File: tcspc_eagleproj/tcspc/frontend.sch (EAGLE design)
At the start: 91 parts, among them Q2 ALD1101SAL, U1 DS90LV028AQ, U3 ADCMP582, U4 LT6003_SOT23-5, U5 LT6003_SOT23-5, U6 AD53X8, X1 SMA, X2 SMA

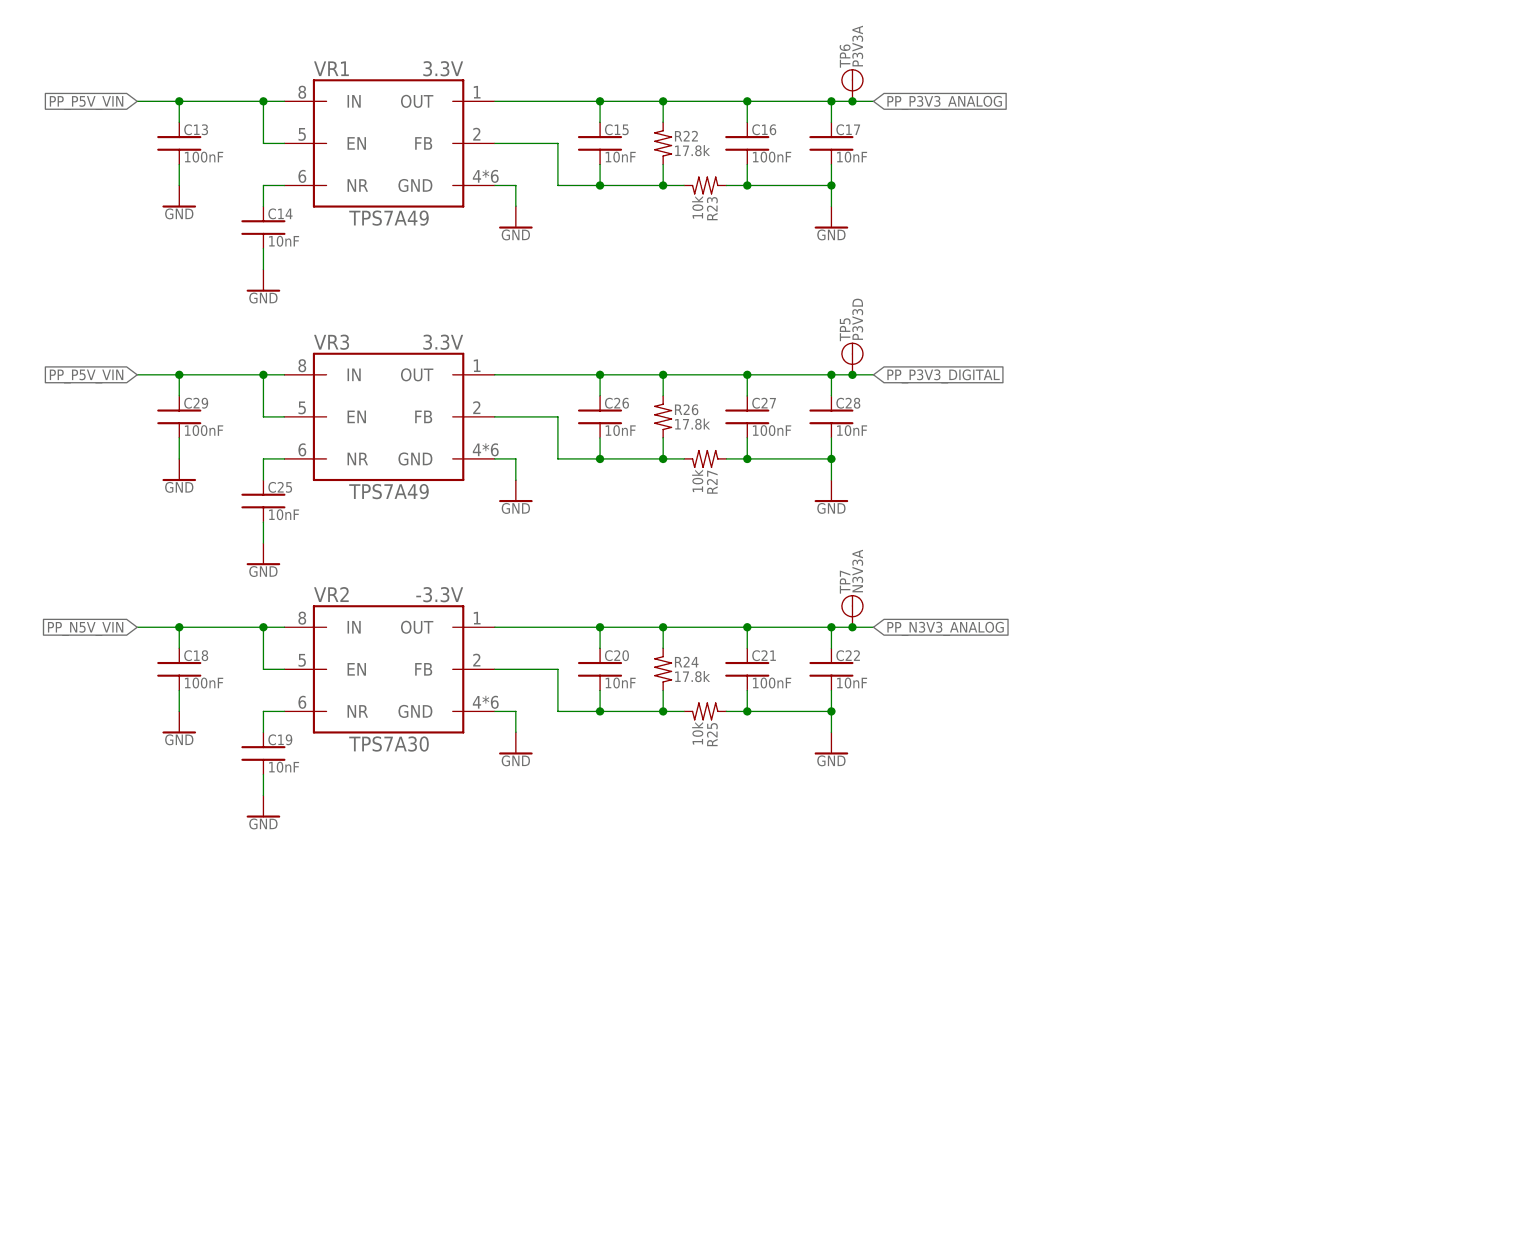
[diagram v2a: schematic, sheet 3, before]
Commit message: stuffed another datasheet into the folder, made some small tweaks to the schematic, created a new brd file and started organizing parts for routing. Fixed the small dot test pad and added a small drill in it for a scope probe
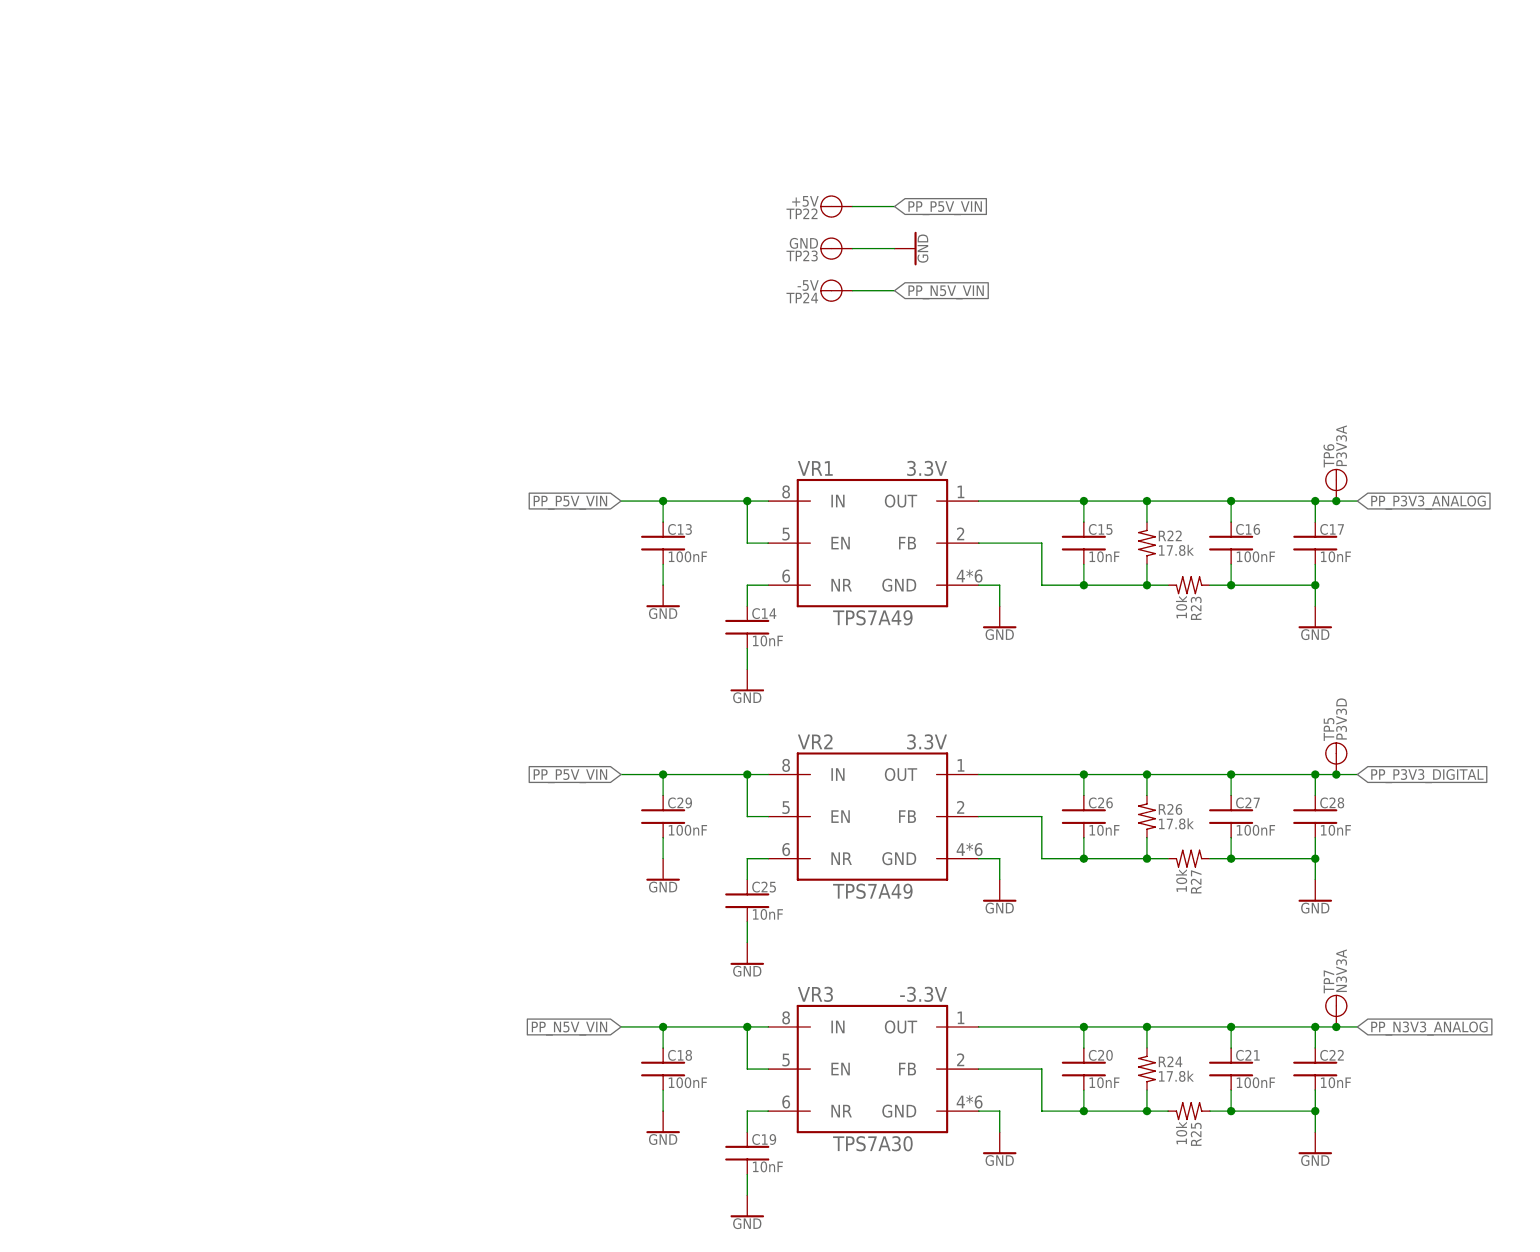
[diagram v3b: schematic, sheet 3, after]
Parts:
- added C4: 100nF, tcspc_lib:CAP_0402
- added TP22: +5V, tcspc_lib:TESTPOINT_A
- added TP23: GND, tcspc_lib:TESTPOINT_A
- added TP24: -5V, tcspc_lib:TESTPOINT_A
- R10, R11: value (none) -> 3.2k
- R12, R13: value (none) -> 1.8k
- R6: value 0 -> 1k
- TP1: value (none) -> DAC_SCLK
- TP18, TP19, TP20, TP21: device tcspc_lib:TESTPOINT_A -> tcspc_lib:TESTPOINT_PAD
- TP2: value (none) -> DAC_!SYNC!
- TP3: value (none) -> DAC_DIN
- TP4: value (none) -> DAC_!LDAC!
- TP8, TP9: value (none) -> GND
- VR2: value -3.3V -> 3.3V; device tcspc_lib:TPS7A30 -> tcspc_lib:TPS7A49
- VR3: value 3.3V -> -3.3V; device tcspc_lib:TPS7A49 -> tcspc_lib:TPS7A30
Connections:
- removed net N$15: U1.OUT-A, X2.1
- removed net N$20: TP9.TP
- new net N$14: U1.OUT-B, X2.1
- new net N$17: C55.1, R6.2, U5.IN+
- net !CHA_LVDS_OUT: now also U1.!IN-B; no longer U1.!IN-A
- net CHA_HYS_SET: now also R6.1; no longer C55.1, U5.IN+
- net CHA_LVDS_OUT: now also U1.IN-B; no longer U1.IN-A
- net CHA_THRESH_SET: now also R5.1; no longer R6.1
- net GND: now also C4.2, TP23.TP, TP8.TP, TP9.TP; no longer R5.2
- net N$16: now also VR2.NR; no longer VR3.NR
- net N$21: now also VR2.FB; no longer VR3.FB
- net N$25: now also VR3.NR; no longer VR2.NR
- net N$4: now also VR3.FB; no longer VR2.FB
- net N$9: now also R5.2; no longer R5.1, R6.2
- net PP_N3V3_ANALOG: now also C4.1, VR3.OUT; no longer VR2.OUT
- net PP_N5V_VIN: now also TP24.TP, VR3.EN, VR3.IN; no longer VR2.EN, VR2.IN
- net PP_P3V3_ANALOG: no longer C11.1
- net PP_P3V3_DIGITAL: now also C11.1, VR2.OUT; no longer VR3.OUT
- net PP_P5V_VIN: now also TP22.TP, VR2.EN, VR2.IN; no longer VR3.EN, VR3.IN
- net T/H_DAC_DIN: no longer TP8.TP
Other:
- moved on the sheet: C11, C12, C13, C14, C15, C16, C17, C18, C19, C20, C21, C22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

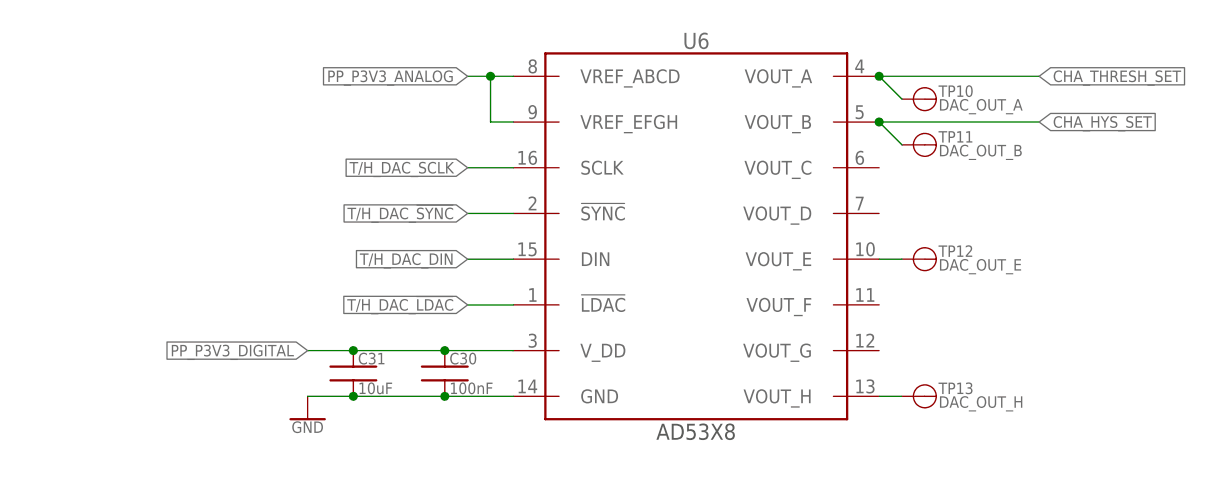
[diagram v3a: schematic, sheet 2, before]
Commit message: Added a termination resistor to the LVDS to TTL reciever, changed a few layers on the SMA coax connector, finished up the board layout, generated gerbers to send to 3PCB.
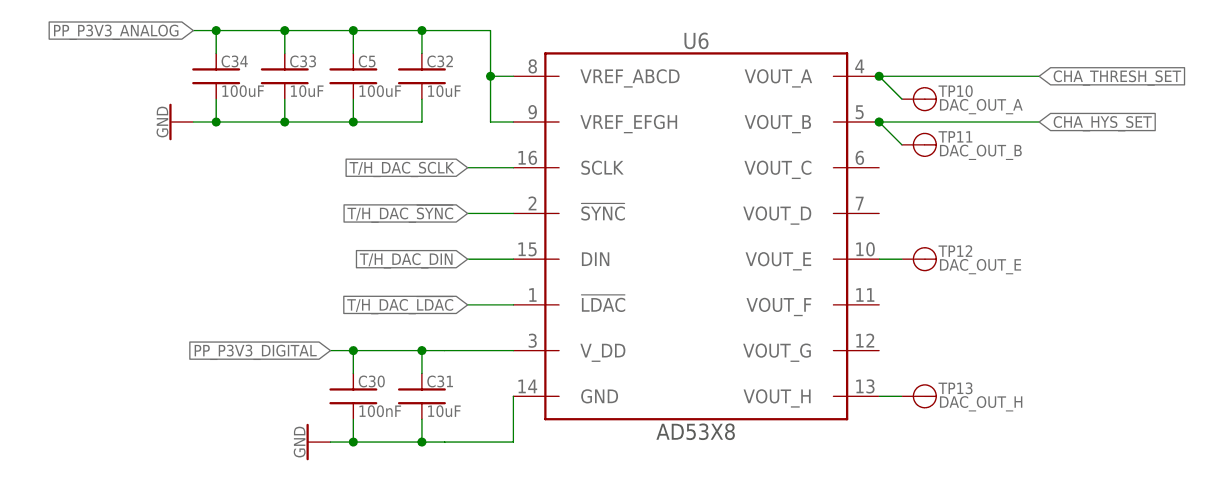
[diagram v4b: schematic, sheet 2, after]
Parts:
- added C32, C33: 10uF, tcspc_lib:CAP_0402
- added C34, C5: 100uF, tcspc_lib:CAP_0402
- added R7: 100, tcspc_lib:RES_0402
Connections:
- removed net N$14: U1.OUT-B, X2.1
- new net N$22: U1.OUT-A, X2.1
- net !CHA_LVDS_OUT: now also R7.2, U1.!IN-A; no longer U1.!IN-B
- net CHA_LVDS_OUT: now also R7.1, U1.IN-A; no longer U1.IN-B
- net GND: now also C32.2, C33.2, C34.2, C5.2
- net PP_P3V3_ANALOG: now also C32.1, C33.1, C34.1, C5.1
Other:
- moved on the sheet: C30, C31, X2
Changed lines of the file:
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@@
 <part name="TP24" library="tcspc_lib" deviceset="TESTPOINT" device="_A" value="-5V"/>
 <part name="GND40" library="tcspc_lib" deviceset="GND" device=""/>
+<part name="C5" library="tcspc_lib" deviceset="CAP" device="_0402" value="100uF"/>
+<part name="C32" library="tcspc_lib" deviceset="CAP" device="_0402" value="10uF"/>
+<part name="GND41" library="tcspc_lib" deviceset="GND" device=""/>
+<part name="C33" library="tcspc_lib" deviceset="CAP" device="_0402" value="10uF"/>
+<part name="C34" library="tcspc_lib" deviceset="CAP" device="_0402" value="100uF"/>
+<part name="R7" library="tcspc_lib" deviceset="RES" device="_0402" value="100"/>
 </parts>
 <sheets>
@@
 <instance part="FRAME1" gate="G$2" x="172.72" y="0"/>
 <instance part="U6" gate="G$1" x="132.08" y="119.38"/>
-<instance part="C30" gate="G$1" x="104.14" y="104.14"/>
-<instance part="C31" gate="G$1" x="93.98" y="104.14"/>
-<instance part="GND39" gate="1" x="88.9" y="99.06"/>
+<instance part="C30" gate="G$1" x="93.98" y="101.6"/>
+<instance part="C31" gate="G$1" x="101.6" y="101.6"/>
+<instance part="GND39" gate="1" x="88.9" y="96.52" rot="R270"/>
 <instance part="TP10" gate="G$1" x="157.48" y="134.62" rot="R270"/>
 <instance part="TP11" gate="G$1" x="157.48" y="129.54" rot="R270"/>
 <instance part="TP12" gate="G$1" x="157.48" y="116.84" rot="R270"/>
 <instance part="TP13" gate="G$1" x="157.48" y="101.6" rot="R270"/>
+<instance part="C5" gate="G$1" x="93.98" y="137.16"/>
+<instance part="C32" gate="G$1" x="101.6" y="137.16"/>
+<instance part="GND41" gate="1" x="73.66" y="132.08" rot="R270"/>
+<instance part="C33" gate="G$1" x="86.36" y="137.16"/>
+<instance part="C34" gate="G$1" x="78.74" y="137.16"/>
 </instances>
 <busses>
@@
 <segment>
 <pinref part="U6" gate="G$1" pin="V_DD"/>
+<label x="91.44" y="106.68" size="1.27" layer="95" rot="R180" xref="yes"/>
+<wire x1="93.98" y1="106.68" x2="101.6" y2="106.68" width="0.1524" layer="91"/>
+<wire x1="101.6" y1="106.68" x2="104.14" y2="106.68" width="0.1524" layer="91"/>
+<wire x1="93.98" y1="106.68" x2="91.44" y2="106.68" width="0.1524" layer="91"/>
+<wire x1="104.14" y1="106.68" x2="111.76" y2="106.68" width="0.1524" layer="91"/>
 <pinref part="C30" gate="G$1" pin="1"/>
-<wire x1="111.76" y1="106.68" x2="104.14" y2="106.68" width="0.1524" layer="91"/>
+<wire x1="93.98" y1="104.14" x2="93.98" y2="106.68" width="0.1524" layer="91"/>
+<junction x="93.98" y="106.68"/>
 <pinref part="C31" gate="G$1" pin="1"/>
-<wire x1="93.98" y1="106.68" x2="104.14" y2="106.68" width="0.1524" layer="91"/>
-<junction x="104.14" y="106.68"/>
-<wire x1="93.98" y1="106.68" x2="88.9" y2="106.68" width="0.1524" layer="91"/>
-<junction x="93.98" y="106.68"/>
-<label x="88.9" y="106.68" size="1.27" layer="95" rot="R180" xref="yes"/>
+<wire x1="101.6" y1="104.14" x2="101.6" y2="106.68" width="0.1524" layer="91"/>
+<junction x="101.6" y="106.68"/>
 </segment>
 </net>
 <net name="GND" class="0">
 <segment>
+<pinref part="C32" gate="G$1" pin="2"/>
+<wire x1="101.6" y1="134.62" x2="101.6" y2="132.08" width="0.1524" layer="91"/>
+<wire x1="101.6" y1="132.08" x2="93.98" y2="132.08" width="0.1524" layer="91"/>
+<pinref part="C5" gate="G$1" pin="2"/>
+<wire x1="93.98" y1="132.08" x2="86.36" y2="132.08" width="0.1524" layer="91"/>
+<wire x1="86.36" y1="132.08" x2="78.74" y2="132.08" width="0.1524" layer="91"/>
+<wire x1="78.74" y1="132.08" x2="76.2" y2="132.08" width="0.1524" layer="91"/>
+<wire x1="93.98" y1="134.62" x2="93.98" y2="132.08" width="0.1524" layer="91"/>
+<junction x="93.98" y="132.08"/>
+<pinref part="GND41" gate="1" pin="GND"/>
+<pinref part="C34" gate="G$1" pin="2"/>
+<wire x1="78.74" y1="134.62" x2="78.74" y2="132.08" width="0.1524" layer="91"/>
+<junction x="78.74" y="132.08"/>
+<pinref part="C33" gate="G$1" pin="2"/>
+<wire x1="86.36" y1="134.62" x2="86.36" y2="132.08" width="0.1524" layer="91"/>
+<junction x="86.36" y="132.08"/>
+</segment>
+<segment>
 <pinref part="U6" gate="G$1" pin="GND"/>
+<wire x1="111.76" y1="101.6" x2="111.76" y2="96.52" width="0.1524" layer="91"/>
+<pinref part="GND39" gate="1" pin="GND"/>
+<wire x1="111.76" y1="96.52" x2="104.14" y2="96.52" width="0.1524" layer="91"/>
+<wire x1="104.14" y1="96.52" x2="101.6" y2="96.52" width="0.1524" layer="91"/>
+<wire x1="101.6" y1="96.52" x2="93.98" y2="96.52" width="0.1524" layer="91"/>
+<wire x1="93.98" y1="96.52" x2="91.44" y2="96.52" width="0.1524" layer="91"/>
 <pinref part="C30" gate="G$1" pin="2"/>
-<wire x1="111.76" y1="101.6" x2="104.14" y2="101.6" width="0.1524" layer="91"/>
+<wire x1="93.98" y1="99.06" x2="93.98" y2="96.52" width="0.1524" layer="91"/>
+<junction x="93.98" y="96.52"/>
 <pinref part="C31" gate="G$1" pin="2"/>
-<wire x1="104.14" y1="101.6" x2="93.98" y2="101.6" width="0.1524" layer="91"/>
-<junction x="104.14" y="101.6"/>
-<wire x1="93.98" y1="101.6" x2="88.9" y2="101.6" width="0.1524" layer="91"/>
-<junction x="93.98" y="101.6"/>
-<pinref part="GND39" gate="1" pin="GND"/>
+<wire x1="101.6" y1="99.06" x2="101.6" y2="96.52" width="0.1524" layer="91"/>
+<junction x="101.6" y="96.52"/>
 </segment>
 </net>
@@
 <pinref part="U6" gate="G$1" pin="VREF_ABCD"/>
 <wire x1="111.76" y1="137.16" x2="109.22" y2="137.16" width="0.1524" layer="91"/>
-<label x="106.68" y="137.16" size="1.27" layer="95" rot="R180" xref="yes"/>
 <pinref part="U6" gate="G$1" pin="VREF_EFGH"/>
-<wire x1="109.22" y1="137.16" x2="106.68" y2="137.16" width="0.1524" layer="91"/>
+<wire x1="109.22" y1="137.16" x2="109.22" y2="142.24" width="0.1524" layer="91"/>
 <wire x1="111.76" y1="132.08" x2="109.22" y2="132.08" width="0.1524" layer="91"/>
 <wire x1="109.22" y1="132.08" x2="109.22" y2="137.16" width="0.1524" layer="91"/>
 <junction x="109.22" y="137.16"/>
+<pinref part="C5" gate="G$1" pin="1"/>
+<wire x1="93.98" y1="139.7" x2="93.98" y2="142.24" width="0.1524" layer="91"/>
+<wire x1="93.98" y1="142.24" x2="86.36" y2="142.24" width="0.1524" layer="91"/>
+<wire x1="86.36" y1="142.24" x2="78.74" y2="142.24" width="0.1524" layer="91"/>
+<wire x1="78.74" y1="142.24" x2="76.2" y2="142.24" width="0.1524" layer="91"/>
+<wire x1="93.98" y1="142.24" x2="101.6" y2="142.24" width="0.1524" layer="91"/>
+<junction x="93.98" y="142.24"/>
+<pinref part="C32" gate="G$1" pin="1"/>
+<wire x1="101.6" y1="142.24" x2="109.22" y2="142.24" width="0.1524" layer="91"/>
+<wire x1="101.6" y1="139.7" x2="101.6" y2="142.24" width="0.1524" layer="91"/>
+<junction x="101.6" y="142.24"/>
+<label x="76.2" y="142.24" size="1.27" layer="95" rot="R180" xref="yes"/>
+<pinref part="C34" gate="G$1" pin="1"/>
+<wire x1="78.74" y1="139.7" x2="78.74" y2="142.24" width="0.1524" layer="91"/>
+<junction x="78.74" y="142.24"/>
+<pinref part="C33" gate="G$1" pin="1"/>
+<wire x1="86.36" y1="139.7" x2="86.36" y2="142.24" width="0.1524" layer="91"/>
+<junction x="86.36" y="142.24"/>
 </segment>
 </net>
@@
 <sheet>
 <plain>
-<text x="196.85" y="150.368" size="1.27" layer="203" align="bottom-center">50_OHM_SE</text>
+<text x="196.85" y="155.448" size="1.27" layer="203" align="bottom-center">50_OHM_SE</text>
 </plain>
 <instances>
 <instance part="FRAME3" gate="G$1" x="0" y="0"/>
 <instance part="FRAME3" gate="G$2" x="172.72" y="0"/>
-<instance part="X2" gate="G$1" x="205.74" y="149.86" rot="MR0"/>
+<instance part="X2" gate="G$1" x="205.74" y="152.4" rot="MR0"/>
 <instance part="TP3" gate="G$1" x="60.96" y="193.04" rot="MR270"/>
 <instance part="TP4" gate="G$1" x="60.96" y="187.96" rot="MR270"/>
@@
 <instance part="GND8" gate="1" x="71.12" y="177.8" rot="R90"/>
 <instance part="GND9" gate="1" x="71.12" y="172.72" rot="R90"/>
+<instance part="R7" gate="G$1" x="154.94" y="157.48"/>
 </instances>
 <busses>
@@
 <pinref part="GND33" gate="1" pin="GND"/>
 <pinref part="X2" gate="G$1" pin="GND"/>
-<wire x1="203.2" y1="147.32" x2="195.58" y2="147.32" width="0.1524" layer="91"/>
-<wire x1="195.58" y1="147.32" x2="195.58" y2="144.78" width="0.1524" layer="91"/>
+<wire x1="203.2" y1="149.86" x2="195.58" y2="149.86" width="0.1524" layer="91"/>
+<wire x1="195.58" y1="149.86" x2="195.58" y2="144.78" width="0.1524" layer="91"/>
 <junction x="195.58" y="144.78"/>
 </segment>
@@
 <net name="CHA_LVDS_OUT" class="2">
 <segment>
-<pinref part="U1" gate="G$1" pin="IN-B"/>
-<wire x1="160.02" y1="149.86" x2="154.94" y2="149.86" width="0.1524" layer="91"/>
-<label x="154.94" y="149.86" size="1.27" layer="95" rot="R180" xref="yes"/>
+<pinref part="U1" gate="G$1" pin="IN-A"/>
+<wire x1="160.02" y1="160.02" x2="154.94" y2="160.02" width="0.1524" layer="91"/>
+<label x="152.4" y="160.02" size="1.27" layer="95" rot="R180" xref="yes"/>
+<pinref part="R7" gate="G$1" pin="1"/>
+<wire x1="154.94" y1="160.02" x2="152.4" y2="160.02" width="0.1524" layer="91"/>
+<junction x="154.94" y="160.02"/>
 </segment>
 </net>
 <net name="!CHA_LVDS_OUT" class="2">
 <segment>
-<pinref part="U1" gate="G$1" pin="!IN-B"/>
-<wire x1="160.02" y1="144.78" x2="154.94" y2="144.78" width="0.1524" layer="91"/>
-<label x="154.94" y="144.78" size="1.27" layer="95" rot="R180" xref="yes"/>
+<pinref part="U1" gate="G$1" pin="!IN-A"/>
+<wire x1="160.02" y1="154.94" x2="154.94" y2="154.94" width="0.1524" layer="91"/>
+<label x="152.4" y="154.94" size="1.27" layer="95" rot="R180" xref="yes"/>
+<pinref part="R7" gate="G$1" pin="2"/>
+<wire x1="154.94" y1="154.94" x2="152.4" y2="154.94" width="0.1524" layer="91"/>
+<junction x="154.94" y="154.94"/>
 </segment>
 </net>
@@
 </segment>
 </net>
-<net name="N$14" class="1">
-<segment>
-<pinref part="U1" gate="G$1" pin="OUT-B"/>
-<wire x1="203.2" y1="149.86" x2="190.5" y2="149.86" width="0.1524" layer="91"/>
+<net name="N$22" class="1">
+<segment>
+<pinref part="U1" gate="G$1" pin="OUT-A"/>
+<wire x1="190.5" y1="154.94" x2="203.2" y2="154.94" width="0.1524" layer="91"/>
 <pinref part="X2" gate="G$1" pin="1"/>
-</segment>
-</net>
+<wire x1="203.2" y1="152.4" x2="203.2" y2="154.94" width="0.1524" layer="91"/>
+</segment>
+</net>
